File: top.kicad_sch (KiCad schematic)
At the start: 5 parts, among them IC1 ADE-2ASK+, J1 PCB.SMAFRA.HT, J2 PCB.SMAFRA.HT, J3 PCB.SMAFRA.HT

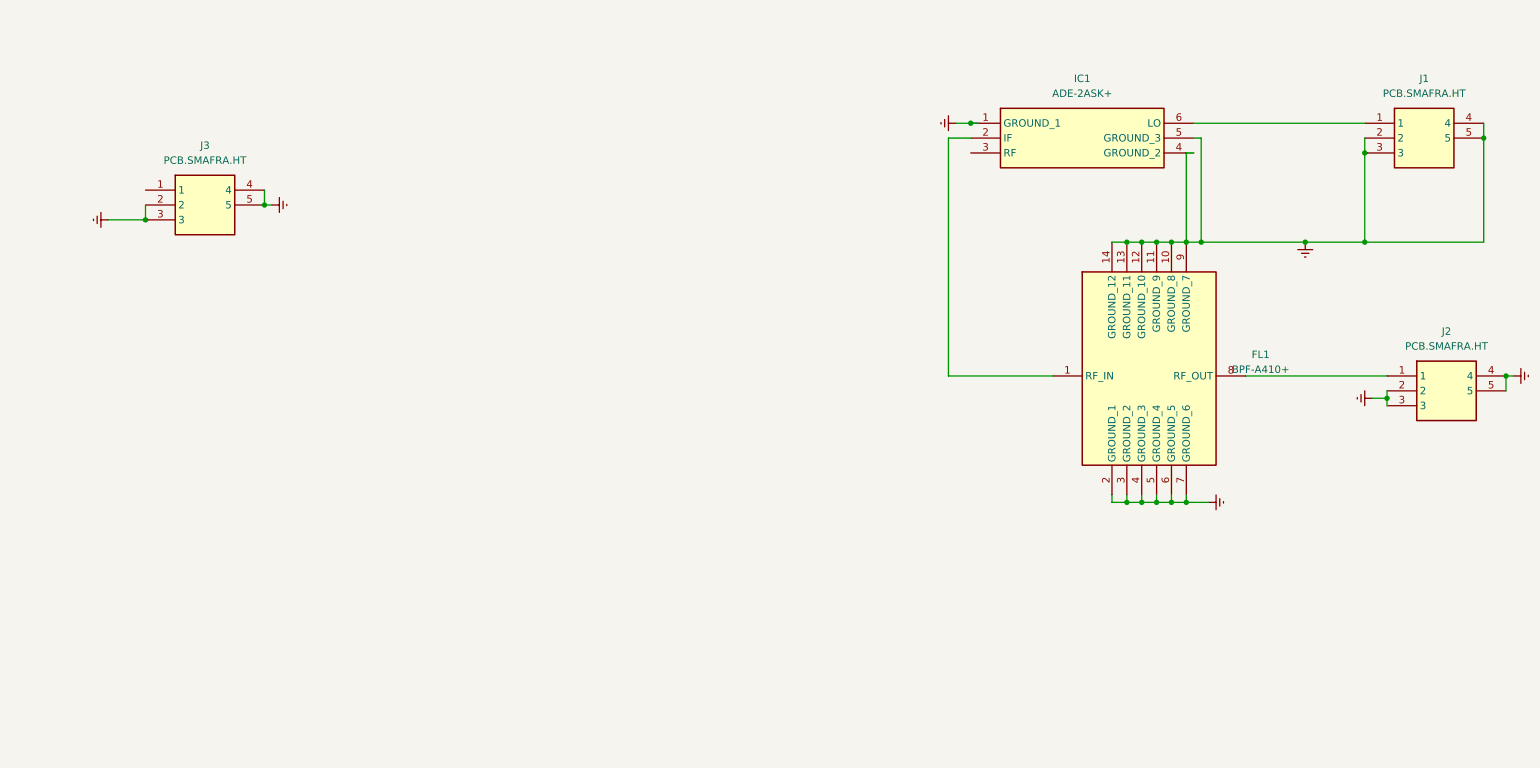
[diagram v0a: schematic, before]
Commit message: Redefined filters & Top Level Diagram
- Implement wider filters to accomodate 10% tolerance parts.
- Break design in to top-level heirarchical blocks.
- Start wiring some of the blocks together.
- Add L-Band segment, but is currently just a copy of the UHF filter.
- Add the start of a TX path.
- Add placeholders for power and band/tune control.
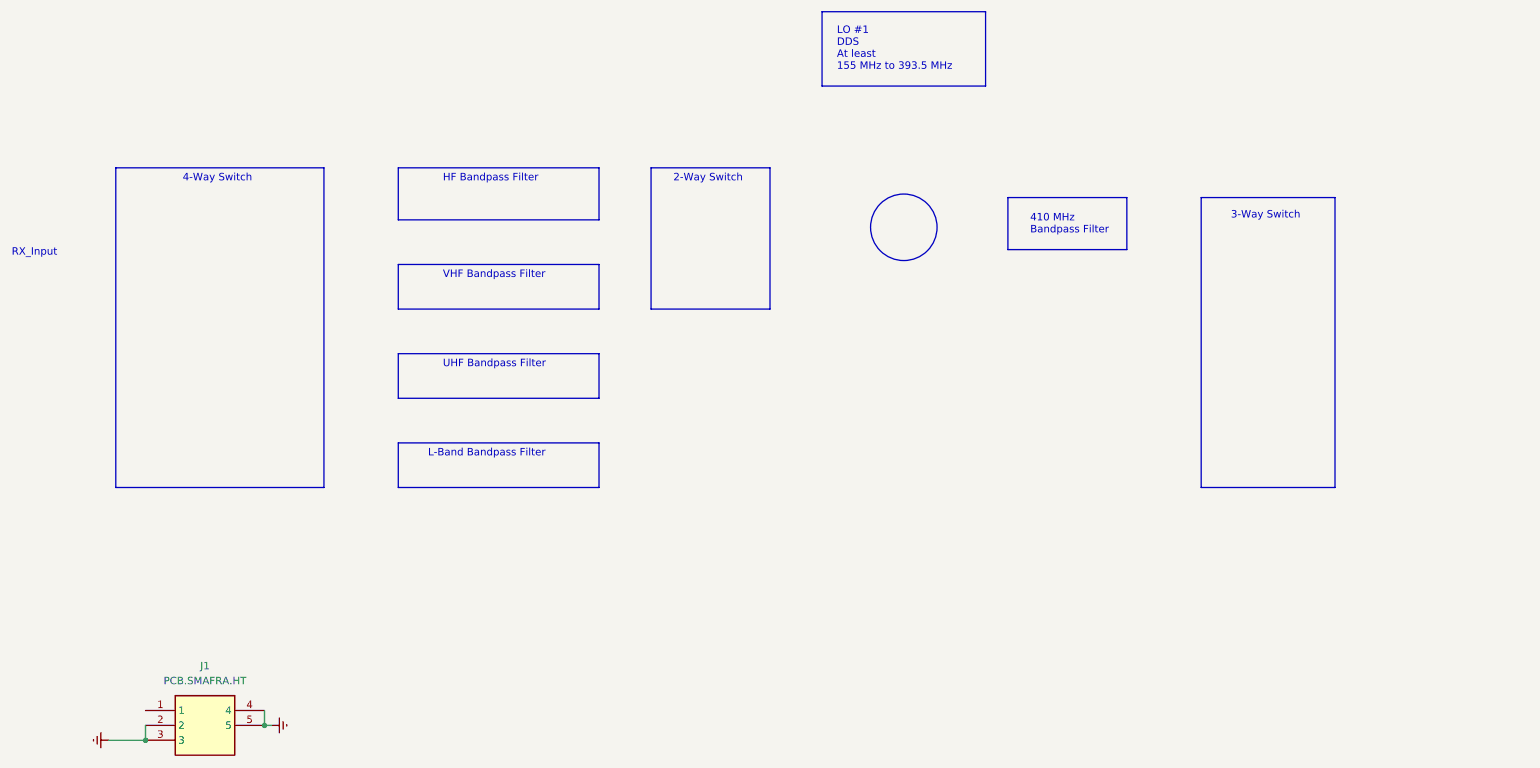
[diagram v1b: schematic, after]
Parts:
- removed FL1: BPF-A410+, SamacSys_Parts:BPFA410, symbol SamacSys_Parts:BPF-A410+
- removed IC1: ADE-2ASK+, SamacSys_Parts:ADE2ASK, symbol SamacSys_Parts:ADE-2ASK+
- removed J2, J3: PCB.SMAFRA.HT, SamacSys_Parts:PCBSMAFRAHT, symbol SamacSys_Parts:PCB.SMAFRA.HT
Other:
- note added: "2-Way Switch"
- note added: "3-Way Switch"
- note added: "4-Way Switch"
- note added: "410 MHz Bandpass Filter"
- note added: "HF Bandpass Filter"
- note added: "L-Band Bandpass Filter"
- note added: "LO #1 DDS At least 155 MHz to 393.5 MHz"
- note added: "RX_Input"
- note added: "UHF Bandpass Filter"
- note added: "VHF Bandpass Filter"
